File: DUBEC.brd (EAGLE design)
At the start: 39 x 21.4 mm, 51 parts

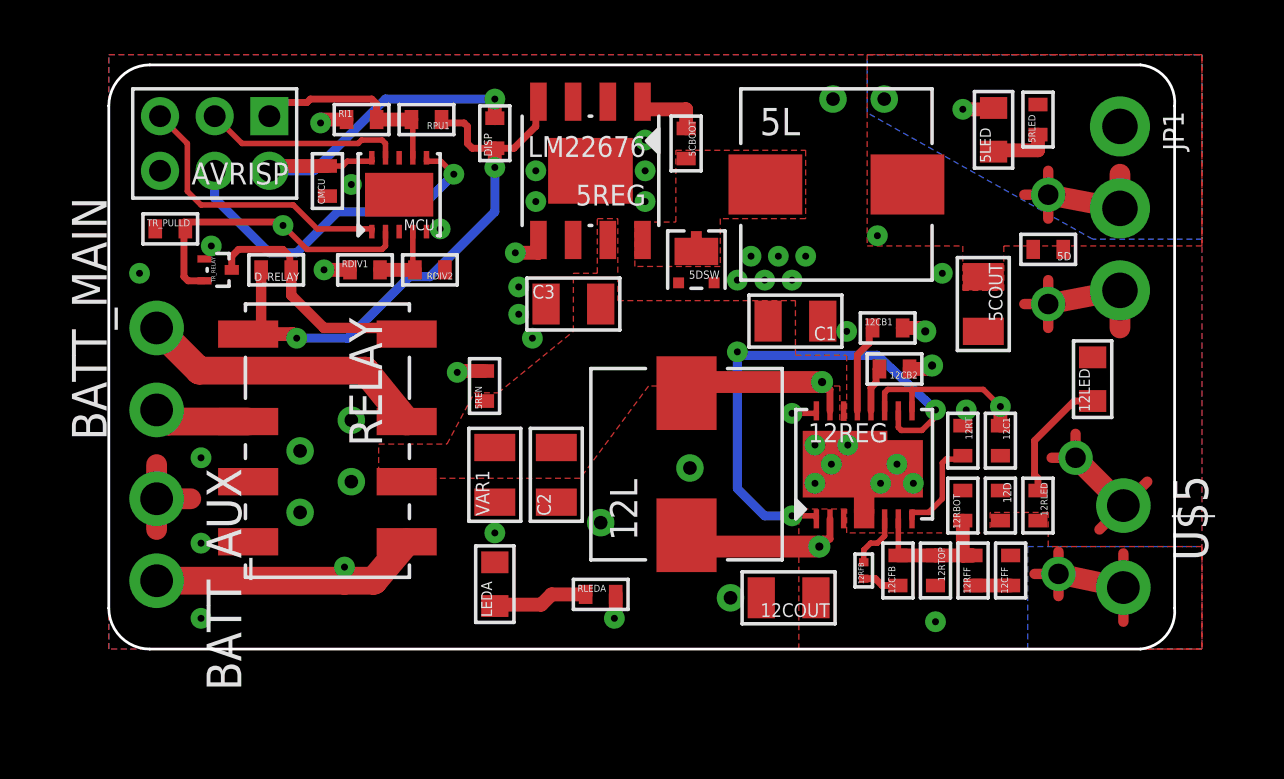
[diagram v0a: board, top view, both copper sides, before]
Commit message: Used space for a cap; tidying
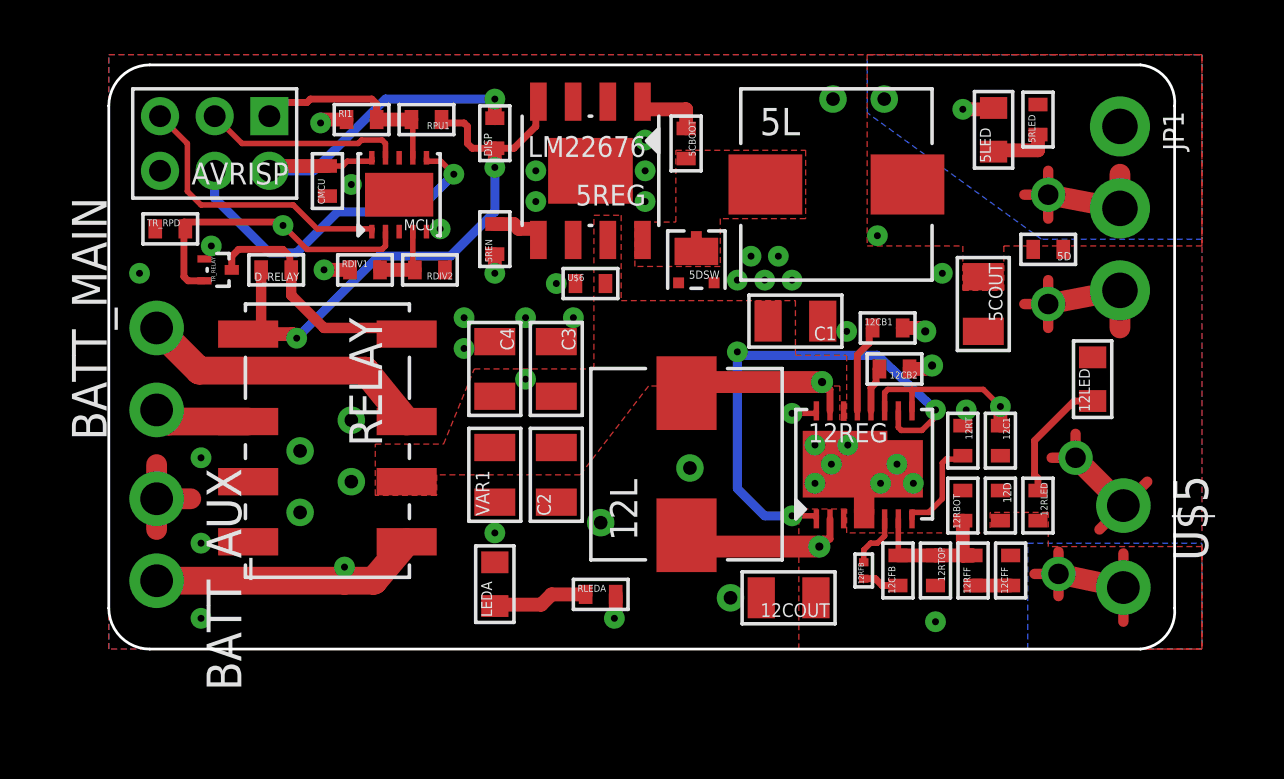
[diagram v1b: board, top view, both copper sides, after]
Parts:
- added C4: 22uF, dubec:0805
- added U$6: (no value), dubec:0402
- 12RBOT: value 90.9kOhm -> RES90.9K_16
- 12RFF: value 10kOhm -> RES10K_8
- 12RLED: value 2.2kOhm -> RES2.2K_8
- RDIV1: value RES26.7K_16 -> RES90.9K_16
- RDIV2: value RES4.22K_16 -> RES15.4K_16
- RPU1: value RES1K_8 -> RES2.2K_8
- TR_RPD: value RES2K_8 -> RES10K_8
- moved 5REN 5.39 mm to (14.1, 15.0)
- moved C3 2.46 mm to (16.4, 10.2), turned to 270 degrees
- renumbered TR_PULLD to TR_RPD
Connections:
- net 35V: now also C4.2, U$6.2
- net GND: now also C4.1, U$6.1
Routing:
- net 5EN: track 7.59 -> 2.07 mm, vias 2 -> 0
- net 35V: track 19.1 -> 24.3 mm, vias 3 -> 5
- net GND: vias 42 -> 43

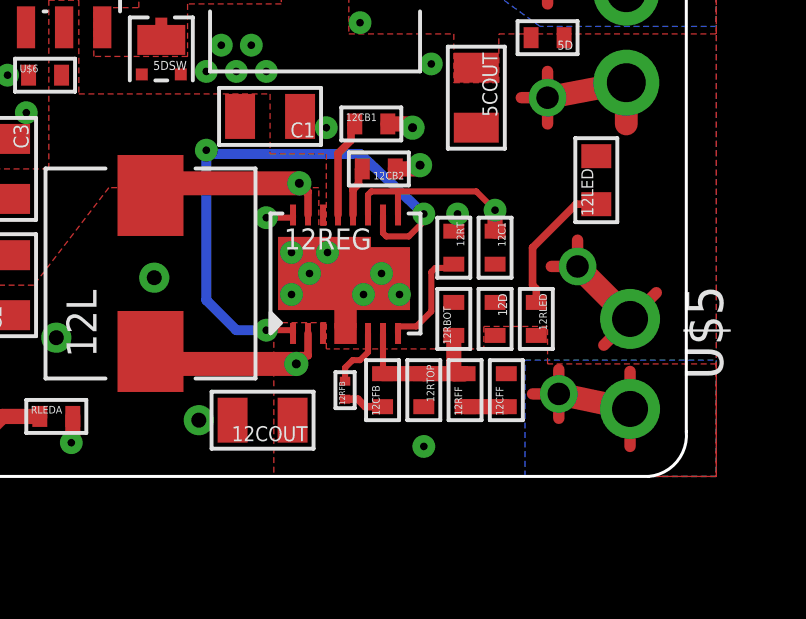
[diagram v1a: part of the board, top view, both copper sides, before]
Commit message: Replaced final 0201 component
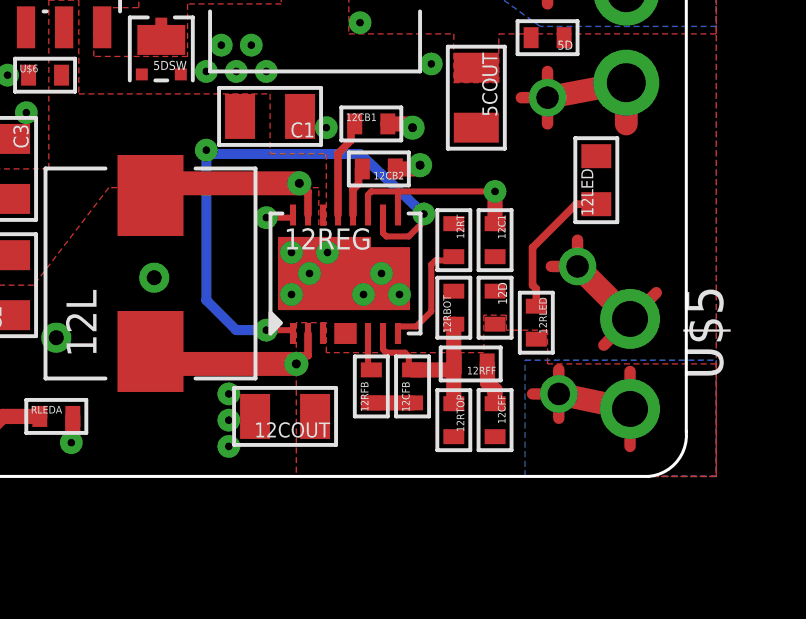
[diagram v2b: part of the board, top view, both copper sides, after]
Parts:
- 12RFB: device dubec:0201P -> dubec:0402
- moved 12RTOP 1.41 mm to (31.2, 1.88)
- moved 12CFF 1.07 mm to (32.6, 1.88), turned to 270 degrees
- moved 12CFB 1.01 mm to (29.9, 3.00)
- moved 12RFF 0.89 mm to (31.8, 3.75), turned to 180 degrees
- moved 12RFB 0.88 mm to (28.5, 3.00)
- moved 12COUT 0.76 mm to (25.6, 2.00)
- moved 12D 0.38 mm to (32.6, 5.62)
- moved 12RBOT 0.38 mm to (31.2, 5.62)
- moved 12C1 0.25 mm to (32.6, 7.88)
- moved 12RT 0.25 mm to (31.2, 7.88)
- moved 12RLED 0.12 mm to (34.0, 5.12)
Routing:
- net 12V_COMP: track 2.05 -> 1.24 mm
- net GND: track 17.8 -> 17.2 mm
- net 12VCC: track 21.0 -> 20.5 mm

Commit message: Layout tweak
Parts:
- moved 12RLED 0.12 mm to (34.0, 5.00)
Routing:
- net GND: vias 43 -> 44
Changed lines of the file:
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@@
 <attribute name="TEMP" value="±200ppm/°C" x="18" y="2" size="1.778" layer="27" display="off"/>
 </element>
-<element name="12RLED" library="dubec" package="0402" value="RES2.2K_8" x="34" y="5.125" rot="R270">
-<attribute name="DIGIKEY_PART_#" value="541-2.2KYACT-ND" x="34" y="5.125" size="1.778" layer="27" rot="R270" display="off"/>
-<attribute name="MANUFACTURER" value="Vishay Dale" x="34" y="5.125" size="1.778" layer="27" rot="R270" display="off"/>
-<attribute name="MFG_PART_#" value="CRCW04022K20JNEDHP" x="34" y="5.125" size="1.778" layer="27" rot="R270" display="off"/>
-<attribute name="USD" value="1.44/10" x="34" y="5.125" size="1.778" layer="27" rot="R270" display="off"/>
-<attribute name="TOLERANCE" value="±5%" x="34" y="5.125" size="1.778" layer="27" rot="R270" display="off"/>
-<attribute name="TEMP" value="±200ppm/°C" x="34" y="5.125" size="1.778" layer="27" rot="R270" display="off"/>
+<element name="12RLED" library="dubec" package="0402" value="RES2.2K_8" x="34" y="5" rot="R270">
+<attribute name="DIGIKEY_PART_#" value="541-2.2KYACT-ND" x="34" y="5" size="1.778" layer="27" rot="R270" display="off"/>
+<attribute name="MANUFACTURER" value="Vishay Dale" x="34" y="5" size="1.778" layer="27" rot="R270" display="off"/>
+<attribute name="MFG_PART_#" value="CRCW04022K20JNEDHP" x="34" y="5" size="1.778" layer="27" rot="R270" display="off"/>
+<attribute name="USD" value="1.44/10" x="34" y="5" size="1.778" layer="27" rot="R270" display="off"/>
+<attribute name="TOLERANCE" value="±5%" x="34" y="5" size="1.778" layer="27" rot="R270" display="off"/>
+<attribute name="TEMP" value="±200ppm/°C" x="34" y="5" size="1.778" layer="27" rot="R270" display="off"/>
 </element>
 <element name="5RLED" library="dubec" package="0402" value="470Ohm" x="34" y="19.375" rot="R90">
@@
 <via x="23.75" y="1.875" extent="1-16" drill="0.254"/>
 <via x="23.75" y="2.75" extent="1-16" drill="0.254"/>
+<via x="31.25" y="10.625" extent="1-16" drill="0.254"/>
 <wire x1="37.125" y1="5.25" x2="36.25" y2="4.375" width="0" layer="19" extent="1-1"/>
 </signal>
@@
 <vertex x="40" y="3.75"/>
 <vertex x="34.375" y="3.75"/>
-<vertex x="34.375" y="4.875"/>
-<vertex x="33" y="4.875"/>
+<vertex x="34.375" y="4.75"/>
+<vertex x="33" y="4.75"/>
 <vertex x="33" y="5.375"/>
 <vertex x="32.25" y="5.375"/>
@@
 <wire x1="37.125" y1="2.25" x2="37.125" y2="1" width="0.381" layer="1"/>
 <wire x1="33.875" y1="2.75" x2="34.75" y2="2.75" width="0.381" layer="1"/>
-<wire x1="34.75" y1="3.5625" x2="34" y2="4.575" width="0" layer="19" extent="1-1"/>
+<wire x1="34.75" y1="3.5625" x2="34" y2="4.45" width="0" layer="19" extent="1-1"/>
 </signal>
 <signal name="5V">
@@
 <contactref element="12LED" pad="A"/>
 <contactref element="12RLED" pad="1"/>
-<wire x1="34" y1="5.675" x2="34" y2="6.25" width="0.254" layer="1"/>
-<wire x1="34" y1="6.25" x2="33.875" y2="6.375" width="0.254" layer="1"/>
-<wire x1="33.875" y1="6.375" x2="33.875" y2="7.625" width="0.254" layer="1"/>
-<wire x1="33.875" y1="7.625" x2="35.325" y2="9.075" width="0.254" layer="1"/>
-<wire x1="35.325" y1="9.075" x2="36" y2="9.075" width="0.254" layer="1"/>
+<wire x1="34" y1="5.55" x2="34" y2="6" width="0.254" layer="1"/>
+<wire x1="34" y1="6" x2="33.75" y2="6.25" width="0.254" layer="1"/>
+<wire x1="33.75" y1="6.25" x2="33.75" y2="7.625" width="0.254" layer="1"/>
+<wire x1="33.75" y1="7.625" x2="35.2" y2="8.95" width="0.254" layer="1"/>
+<wire x1="35.2" y1="8.95" x2="36" y2="9.075" width="0.254" layer="1"/>
 </signal>
 <signal name="SCK">
@@
 <contactref element="RPU1" pad="2"/>
 <contactref element="MCU" pad="7"/>
-<wire x1="9.625" y1="20.125" x2="7.375" y2="20.125" width="0.254" layer="1"/>
-<wire x1="7.375" y1="20.125" x2="7.25" y2="20" width="0.254" layer="1"/>
-<wire x1="7.25" y1="20" x2="6.5" y2="20" width="0.254" layer="1"/>
+<wire x1="9.625" y1="20.125" x2="7.25" y2="20.125" width="0.254" layer="1"/>
+<wire x1="7.25" y1="20.125" x2="7.125" y2="20" width="0.254" layer="1"/>
+<wire x1="7.125" y1="20" x2="6.5" y2="20" width="0.254" layer="1"/>
 <wire x1="6.5" y1="20" x2="5.875" y2="19.5" width="0.254" layer="1"/>
 <wire x1="9.625" y1="20.125" x2="9.8" y2="19.95" width="0.254" layer="1"/>

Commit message: Cream update
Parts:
- moved 12CFB 0.12 mm to (29.9, 2.88)
- moved 12RFB 0.12 mm to (28.5, 2.88)
- renumbered U$6 to 5CIN
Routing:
- net GND: vias 44 -> 48
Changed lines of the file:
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@@
 <attribute name="TEMP" value="C0G, NP0" x="32.625" y="1.875" size="1.778" layer="27" rot="R270" display="off"/>
 </element>
-<element name="12RFB" library="dubec" package="0402" value="40.2kOhm" x="28.5" y="3" rot="R90">
-<attribute name="DIGIKEY_PART_#" value="541-40.2KLCT-ND" x="28.5" y="3" size="1.778" layer="27" rot="R90" display="off"/>
-<attribute name="MANUFACTURER" value="Vishay Dale" x="28.5" y="3" size="1.778" layer="27" rot="R90" display="off"/>
-<attribute name="MFG_PART_#" value="CRCW040240K2FKED" x="28.5" y="3" size="1.778" layer="27" rot="R90" display="off"/>
-<attribute name="USD" value="2.11/50" x="28.5" y="3" size="1.778" layer="27" rot="R90" display="off"/>
-<attribute name="TOLERANCE" value="±1%" x="28.5" y="3" size="1.778" layer="27" rot="R90" display="off"/>
-<attribute name="TEMP" value="±100ppm/°C" x="28.5" y="3" size="1.778" layer="27" rot="R90" display="off"/>
-</element>
-<element name="12CFB" library="dubec" package="0402" value="820pF" x="29.875" y="3" rot="R90">
-<attribute name="DIGIKEY_PART_#" value="720-1209-1-ND" x="29.875" y="3" size="1.778" layer="27" rot="R90" display="off"/>
-<attribute name="MANUFACTURER" value="Vishay Vitramon" x="29.875" y="3" size="1.778" layer="27" rot="R90" display="off"/>
-<attribute name="MFG_PART_#" value="VJ0402Y821KNAAJ" x="29.875" y="3" size="1.778" layer="27" rot="R90" display="off"/>
-<attribute name="USD" value="0.43" x="29.875" y="3" size="1.778" layer="27" rot="R90" display="off"/>
-<attribute name="TOLERANCE" value="±10%" x="29.875" y="3" size="1.778" layer="27" rot="R90" display="off"/>
-<attribute name="TEMP" value="X7R" x="29.875" y="3" size="1.778" layer="27" rot="R90" display="off"/>
+<element name="12RFB" library="dubec" package="0402" value="40.2kOhm" x="28.5" y="2.875" rot="R90">
+<attribute name="DIGIKEY_PART_#" value="541-40.2KLCT-ND" x="28.5" y="2.875" size="1.778" layer="27" rot="R90" display="off"/>
+<attribute name="MANUFACTURER" value="Vishay Dale" x="28.5" y="2.875" size="1.778" layer="27" rot="R90" display="off"/>
+<attribute name="MFG_PART_#" value="CRCW040240K2FKED" x="28.5" y="2.875" size="1.778" layer="27" rot="R90" display="off"/>
+<attribute name="USD" value="2.11/50" x="28.5" y="2.875" size="1.778" layer="27" rot="R90" display="off"/>
+<attribute name="TOLERANCE" value="±1%" x="28.5" y="2.875" size="1.778" layer="27" rot="R90" display="off"/>
+<attribute name="TEMP" value="±100ppm/°C" x="28.5" y="2.875" size="1.778" layer="27" rot="R90" display="off"/>
+</element>
+<element name="12CFB" library="dubec" package="0402" value="820pF" x="29.875" y="2.875" rot="R90">
+<attribute name="DIGIKEY_PART_#" value="720-1209-1-ND" x="29.875" y="2.875" size="1.778" layer="27" rot="R90" display="off"/>
+<attribute name="MANUFACTURER" value="Vishay Vitramon" x="29.875" y="2.875" size="1.778" layer="27" rot="R90" display="off"/>
+<attribute name="MFG_PART_#" value="VJ0402Y821KNAAJ" x="29.875" y="2.875" size="1.778" layer="27" rot="R90" display="off"/>
+<attribute name="USD" value="0.43" x="29.875" y="2.875" size="1.778" layer="27" rot="R90" display="off"/>
+<attribute name="TOLERANCE" value="±10%" x="29.875" y="2.875" size="1.778" layer="27" rot="R90" display="off"/>
+<attribute name="TEMP" value="X7R" x="29.875" y="2.875" size="1.778" layer="27" rot="R90" display="off"/>
 </element>
 <element name="12RTOP" library="dubec" package="0402" value="1MOhm" x="31.25" y="1.875" rot="R270">
@@
 <attribute name="MFG_PART_#" value="C2012JB1V226M125AC" x="14.125" y="10.25" size="1.778" layer="27" rot="R270" display="off"/>
 </element>
-<element name="U$6" library="dubec" package="0402" value="" x="17.625" y="13.375">
+<element name="5CIN" library="dubec" package="0402" value="" x="17.625" y="13.375">
 <attribute name="USD" value="0.28" x="17.625" y="13.375" size="1.778" layer="27" display="off"/>
 <attribute name="TOLERANCE" value="±10%" x="17.625" y="13.375" size="1.778" layer="27" display="off"/>
@@
 <wire x1="23.125" y1="10.75" x2="23" y2="10.875" width="0.3302" layer="16"/>
 <contactref element="C4" pad="2"/>
-<contactref element="U$6" pad="2"/>
+<contactref element="5CIN" pad="2"/>
 <via x="14.125" y="13.75" extent="1-16" drill="0.254"/>
 <wire x1="14.125" y1="14.45" x2="14.125" y2="13.75" width="0.508" layer="1"/>
@@
 <contactref element="C4" pad="1"/>
 <via x="17" y="12.125" extent="1-16" drill="0.254"/>
-<contactref element="U$6" pad="1"/>
+<contactref element="5CIN" pad="1"/>
 <via x="16.375" y="13.375" extent="1-16" drill="0.254"/>
 <via x="23.75" y="1" extent="1-16" drill="0.254"/>
@@
 <via x="31.25" y="10.625" extent="1-16" drill="0.254"/>
 <wire x1="37.125" y1="5.25" x2="36.25" y2="4.375" width="0" layer="19" extent="1-1"/>
+<via x="33.25" y="11.125" extent="1-16" drill="0.254"/>
+<via x="17.625" y="17.625" extent="1-16" drill="0.254"/>
+<via x="17.625" y="18.625" extent="1-16" drill="0.254"/>
+<via x="17.625" y="16.625" extent="1-16" drill="0.254"/>
 </signal>
 <signal name="12V">
@@
 <contactref element="12RFF" pad="2"/>
 <wire x1="31.25" y1="5.075" x2="31.25" y2="2.425" width="0.508" layer="1"/>
-<wire x1="29.875" y1="3.55" x2="31.075" y2="3.55" width="0.508" layer="1"/>
+<wire x1="29.875" y1="3.425" x2="31.2" y2="3.425" width="0.508" layer="1"/>
 <wire x1="28.89" y1="4.765" x2="28.89" y2="4.235" width="0.2032" layer="1"/>
-<wire x1="28.89" y1="4.235" x2="29" y2="4.125" width="0.2032" layer="1"/>
-<wire x1="29.625" y1="4.125" x2="29.75" y2="4" width="0.2032" layer="1"/>
-<wire x1="29.75" y1="4" x2="29.75" y2="3.625" width="0.2032" layer="1"/>
-<wire x1="29.75" y1="3.625" x2="29.875" y2="3.625" width="0.2032" layer="1"/>
-<wire x1="29.875" y1="3.625" x2="29.875" y2="3.55" width="0.2032" layer="1"/>
-<wire x1="29.625" y1="4.125" x2="29" y2="4.125" width="0.2032" layer="1"/>
-<wire x1="31.075" y1="3.55" x2="31.2625" y2="3.75" width="0" layer="19" extent="1-1"/>
-<wire x1="31.25" y1="2.425" x2="31.075" y2="3.55" width="0" layer="19" extent="1-1"/>
+<wire x1="28.89" y1="4.235" x2="29.125" y2="4" width="0.2032" layer="1"/>
+<wire x1="29.625" y1="4" x2="29.75" y2="3.875" width="0.2032" layer="1"/>
+<wire x1="29.75" y1="3.875" x2="29.75" y2="3.375" width="0.2032" layer="1"/>
+<wire x1="29.75" y1="3.375" x2="29.875" y2="3.375" width="0.2032" layer="1"/>
+<wire x1="29.875" y1="3.375" x2="29.875" y2="3.425" width="0.2032" layer="1"/>
+<wire x1="29.625" y1="4" x2="29.125" y2="4" width="0.2032" layer="1"/>
+<wire x1="31.2" y1="3.425" x2="31.2625" y2="3.75" width="0" layer="19" extent="1-1"/>
+<wire x1="31.25" y1="2.425" x2="31.2" y2="3.425" width="0" layer="19" extent="1-1"/>
 </signal>
 <signal name="35V_NC">
@@
 <contactref element="12CFB" pad="1"/>
 <contactref element="12RFB" pad="1"/>
-<wire x1="28.5" y1="2.45" x2="29.875" y2="2.45" width="0.508" layer="1"/>
+<wire x1="28.5" y1="2.325" x2="29.875" y2="2.325" width="0.508" layer="1"/>
 </signal>
 <signal name="12V_COMP">
 <contactref element="12RFB" pad="2"/>
 <contactref element="12REG" pad="6"/>
-<wire x1="28.39" y1="4.765" x2="28.39" y2="3.785" width="0.2032" layer="1"/>
-<wire x1="28.39" y1="3.785" x2="28.5" y2="3.55" width="0.2032" layer="1"/>
+<wire x1="28.39" y1="4.765" x2="28.39" y2="3.41" width="0.2032" layer="1"/>
+<wire x1="28.39" y1="3.41" x2="28.5" y2="3.425" width="0.2032" layer="1"/>
 </signal>
 <signal name="N$4">
